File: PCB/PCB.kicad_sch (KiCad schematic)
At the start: 44 parts, among them J1 440054-2, J2 USB_C_Receptacle_PowerOnly_6P, Q1 IRLML6402, Q2 IRLML6402, Q3 2N3904, Q4 2N3904, SW1 SW_SPDT_312, U1 DRV8833PWPR, U2 DRV8833PWPR, U3 INA219AxD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

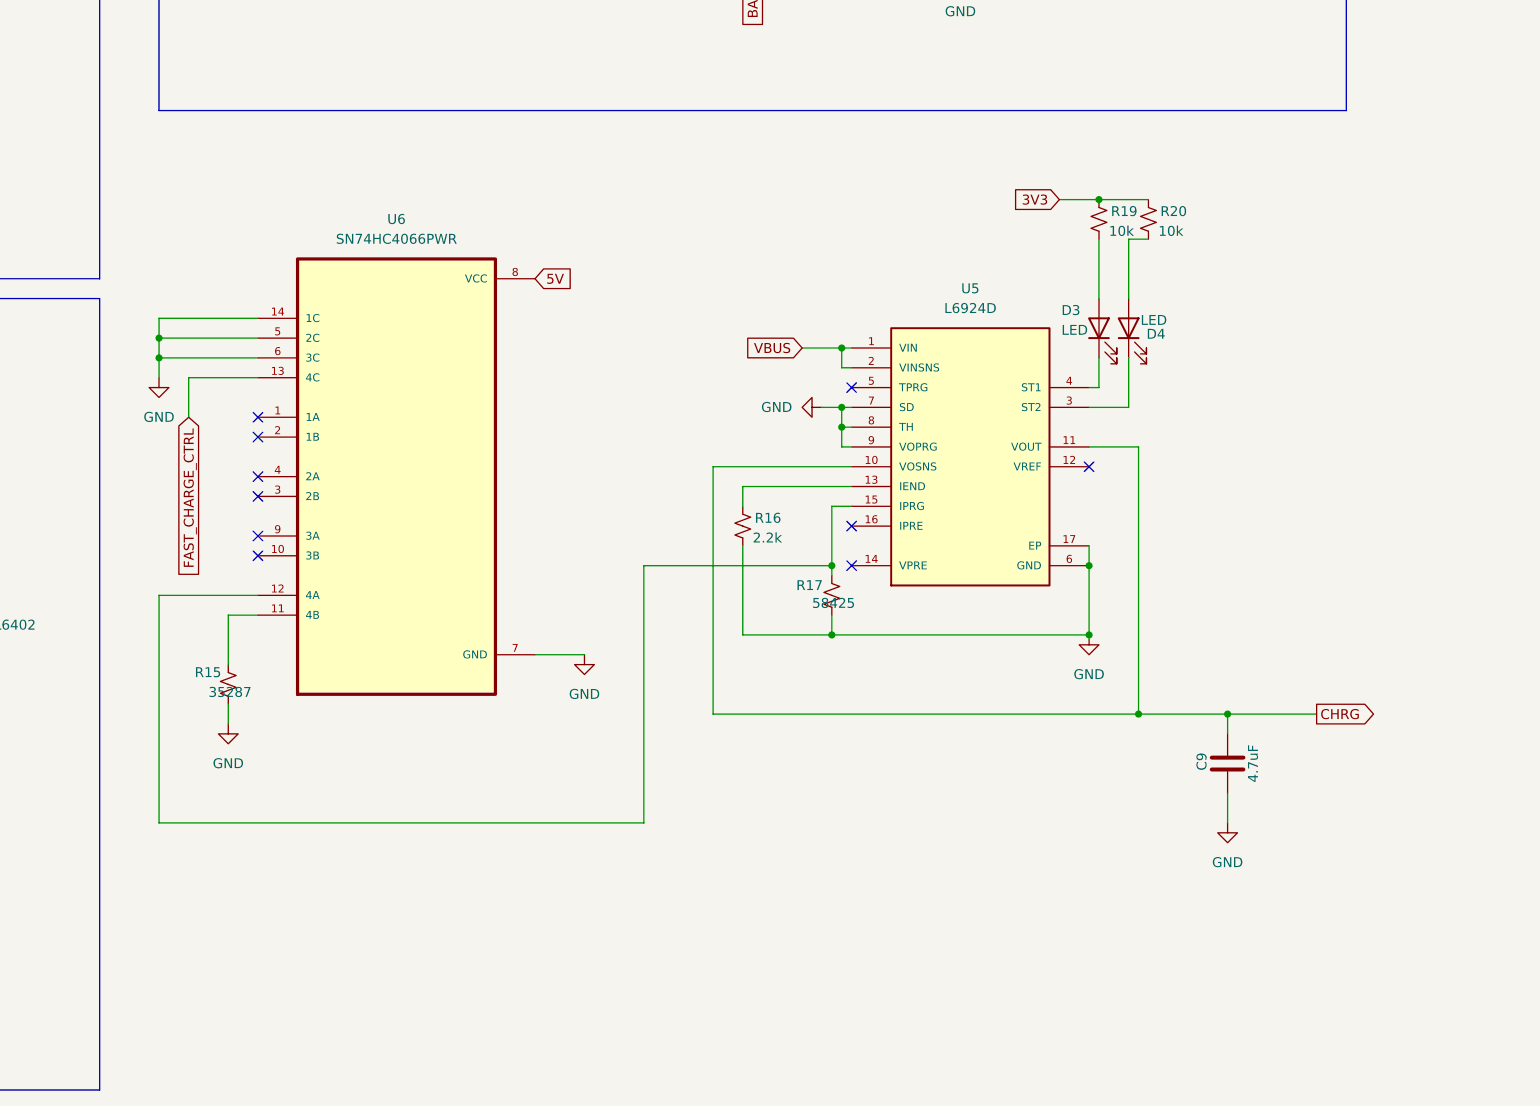
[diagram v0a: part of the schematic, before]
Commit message: Change the charger and fast charging
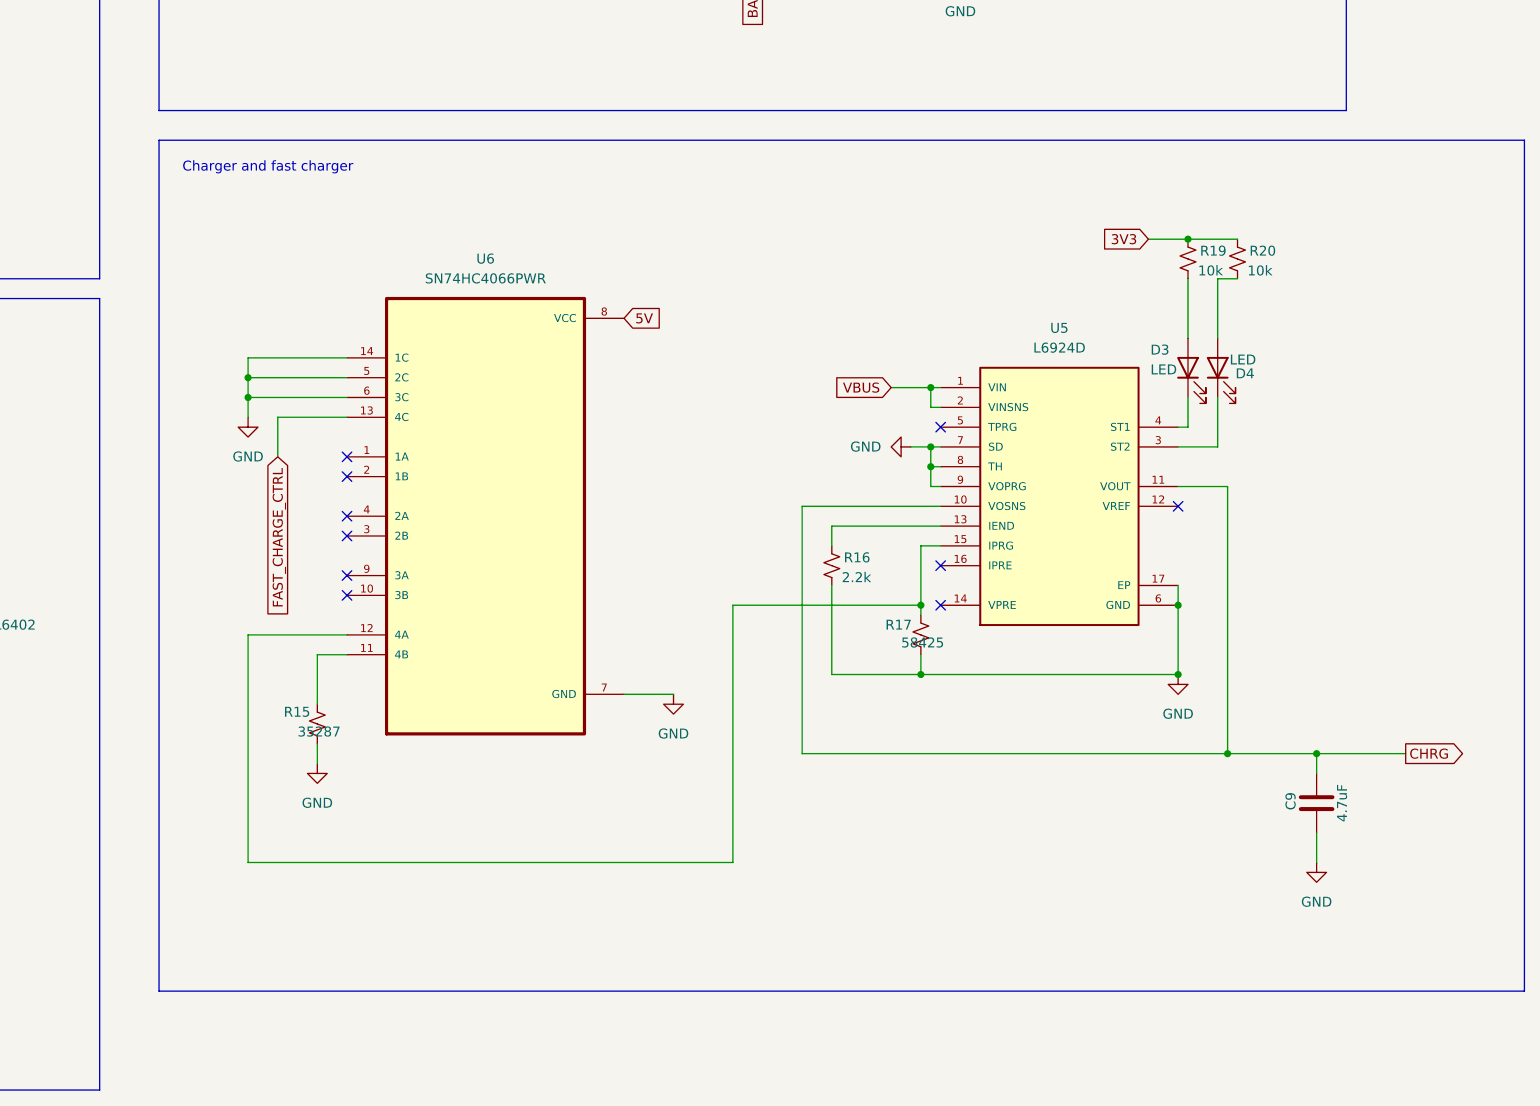
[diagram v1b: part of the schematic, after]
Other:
- note added: "Charger and fast charger"
- moved on the sheet: C9, D3, D4, R15, R16, R17, R19, R20, U5, U6

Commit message: 3V3 and 5V
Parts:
- added C10, C11, C12, C13, C8: 22uF, symbol Device:C
- added D5, D6: D, symbol Device:D
- added L1, L2: 22uF, symbol Device:L
- added R18, R22: 72.3k, symbol Device:R_Small_US
- added R21, R23: 10k, symbol Device:R_Small_US
- added R24: 600, symbol Device:R_Small_US
- added R25: 1000, symbol Device:R_Small_US
- added U7, U8: MT3608, MT3608:SOT95P280X145-6N, symbol MT3608:MT3608
- added U9: AMS1117-3.3, AMS1117-3.3:SOT229P700X180-4N, symbol AMS1117-3.3:AMS1117-3.3
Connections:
- net 3V3: now also R24.1, U9.2 (VOUT)
- net 5V: now also C10.1, D5.1 (K), R18.1
- net BATT: now also C11.1, C13.1, C8.1, L1.1, L2.1, U7.4 (EN), U7.5 (IN), U8.4 (EN), U8.5 (IN), U9.3 (VIN)
- net GND: now also C10.2, C11.2, C12.2, C13.2, C8.2, R21.2, R23.2, R25.2, U7.2 (GND), U8.2 (GND)
- new net: R24.2, R25.1, U9.1 (ADJ/GND)
- new net: D6.2 (A), L2.2, U8.1 (SW)
- new net: R22.2, R23.1, U8.3 (FB)
- new net: D5.2 (A), L1.2, U7.1 (SW)
- new net: R18.2, R21.1, U7.3 (FB)
- new net 5V_2: C12.1, D6.1 (K), R22.1

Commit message: Added switch
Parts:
- removed SW1: SW_SPDT_312, symbol Switch:SW_SPDT_312
- added SW1: SS-12D10G5, SS-12D10G5_XKB, symbol 2025-03-27_23-01-30:SS-12D10G5
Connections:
- net CHRG: now also SW1.2
- net at R9.1, U3.8 (IN+): now also SW1.3
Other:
- note added: "Motor drivers"
- moved on the sheet: C10, C11, C12, C13, C8, D5, D6, L1, L2, R18, R21, R22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

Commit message: FOOTPRINTS
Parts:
- removed D5, D6: D, symbol Device:D
- added J3: Conn_02x16_Odd_Even, symbol Connector_Generic:Conn_02x16_Odd_Even
- added JP1: Jumper_2_Open, symbol Jumper:Jumper_2_Open
- C1, C4: value C -> 10u; footprint (none) -> Capacitor_SMD:C_1206_3216Metric_Pad1.33x1.80mm_HandSolder; LCSC (none) -> C13585
- C10, C11, C12, C13, C8: footprint (none) -> Capacitor_SMD:C_1206_3216Metric_Pad1.33x1.80mm_HandSolder; LCSC (none) -> C12891
- C2, C6: value C -> 0.01u; footprint (none) -> Capacitor_SMD:C_1206_3216Metric_Pad1.33x1.80mm_HandSolder; LCSC (none) -> C1846
- C3, C5: value 10u -> 2.2u; footprint (none) -> Capacitor_SMD:C_1206_3216Metric_Pad1.33x1.80mm_HandSolder; LCSC (none) -> C50254
- C7: footprint (none) -> Capacitor_SMD:C_1206_3216Metric_Pad1.33x1.80mm_HandSolder; LCSC (none) -> C1848
- C9: footprint (none) -> Capacitor_SMD:C_1206_3216Metric_Pad1.33x1.80mm_HandSolder; LCSC (none) -> C29823
- D1, D2, D3, D4: footprint (none) -> LED_SMD:LED_0603_1608Metric_Pad1.05x0.95mm_HandSolder; LCSC (none) -> C2286
- R1, R19, R20, R3, R6, R7: footprint (none) -> Resistor_SMD:R_0603_1608Metric_Pad0.98x0.95mm_HandSolder; LCSC (none) -> C25804
- R10, R11: footprint (none) -> Resistor_SMD:R_0603_1608Metric_Pad0.98x0.95mm_HandSolder; LCSC (none) -> C23162
- R12, R21, R23: footprint (none) -> Resistor_SMD:R_0201_0603Metric_Pad0.64x0.40mm_HandSolder; LCSC (none) -> C25804
- R13, R2, R4, R5, R8: footprint (none) -> Resistor_SMD:R_0603_1608Metric_Pad0.98x0.95mm_HandSolder; LCSC (none) -> C21190
- R14: footprint (none) -> Resistor_SMD:R_0603_1608Metric_Pad0.98x0.95mm_HandSolder; LCSC (none) -> C23212
- R15: value 35287 -> 33k; footprint (none) -> Resistor_SMD:R_0603_1608Metric_Pad0.98x0.95mm_HandSolder; LCSC (none) -> C4216
- R16: footprint (none) -> Resistor_SMD:R_0603_1608Metric_Pad0.98x0.95mm_HandSolder; LCSC (none) -> C4190
- R17: value 58425 -> 56k; footprint (none) -> Resistor_SMD:R_0603_1608Metric_Pad0.98x0.95mm_HandSolder; LCSC (none) -> C23206
- R18, R22: value 72.3k -> 75k; footprint (none) -> Resistor_SMD:R_0201_0603Metric_Pad0.64x0.40mm_HandSolder; LCSC (none) -> C23242
- R24: value 600 -> 6.2k; footprint (none) -> Resistor_SMD:R_0603_1608Metric_Pad0.98x0.95mm_HandSolder; LCSC (none) -> C4260
- R25: value 1000 -> 10k; footprint (none) -> Resistor_SMD:R_0201_0603Metric_Pad0.64x0.40mm_HandSolder; LCSC (none) -> C25804
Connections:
- net 3V3: now also J3.18 (Pin_18), JP1.2 (B); no longer U9.2 (VOUT)
- net 5V: now also L1.2, U7.1 (SW), J3.20 (Pin_20)
- net 5V_2: now also L2.2, U8.1 (SW)
- net BATT: now also J3.14 (Pin_14)
- net CTRL_EXT_LOAD1: now also J3.25 (Pin_25)
- net CTRL_EXT_LOAD2: now also J3.7 (Pin_7)
- net EXT_LOAD1_OUT: now also J3.21 (Pin_21)
- net EXT_LOAD2_OUT: now also J3.11 (Pin_11)
- net FAST_CHARGE_CTRL: now also J3.13 (Pin_13)
- net GND: now also J3.19 (Pin_19), J3.23 (Pin_23)
- net I2C1_SCL: now also J3.16 (Pin_16)
- net I2C1_SDA: now also J3.17 (Pin_17)
- net MOTOR1_A_OUT: now also J3.32 (Pin_32)
- net MOTOR1_B_OUT: now also J3.31 (Pin_31)
- net MOTOR1_CTRL1: now also J3.28 (Pin_28)
- net MOTOR1_CTRL2: now also J3.30 (Pin_30)
- net MOTOR2_A_OUT: now also J3.2 (Pin_2)
- net MOTOR2_B_OUT: now also J3.1 (Pin_1)
- net MOTOR2_CTRL1: now also J3.4 (Pin_4)
- net MOTOR2_CTRL2: now also J3.6 (Pin_6)
- net MOTOR3_A_OUT: now also J3.27 (Pin_27)
- net MOTOR3_B_OUT: now also J3.29 (Pin_29)
- net MOTOR3_CTRL1: now also J3.24 (Pin_24)
- net MOTOR3_CTRL2: now also J3.26 (Pin_26)
- net MOTOR4_A_OUT: now also J3.3 (Pin_3)
- net MOTOR4_B_OUT: now also J3.5 (Pin_5)
- net MOTOR4_CTRL1: now also J3.8 (Pin_8)
- net MOTOR4_CTRL2: now also J3.10 (Pin_10)
- net VBUS: now also J3.22 (Pin_22)
- new net: JP1.1 (A), U9.2 (VOUT)
- no-connect marks 17 -> 20
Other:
- moved on the sheet: R24, R25, U9

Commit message: .
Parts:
- removed J1: 440054-2, CONN2_440054-2_TYC, symbol battery conn ul_440054-2:440054-2
- removed JP1: Jumper_2_Open, symbol Jumper:Jumper_2_Open
- removed Q3, Q4: 2N3904, Package_TO_SOT_THT:TO-92_Inline, symbol Transistor_BJT:2N3904
- added J1: Conn_01x02_Pin, symbol Connector:Conn_01x02_Pin
- added Q5, Q6: SS8050-G, SS8050-G:TRANS_SS8050-G, symbol SS8050-G:SS8050-G
- L1, L2: value 22uF -> 22u
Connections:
- net 3V3: now also U9.2 (VOUT)
- net CHRG: now also J1.1 (Pin_1)
- net GND: now also J1.2 (Pin_2), Q5.2, Q6.2
- net at R5.2: now also Q5.1
- net at Q2.1 (G), R7.2: now also Q6.3
- net at R8.1: now also Q6.1
- net at Q1.1 (G), R6.2: now also Q5.3
